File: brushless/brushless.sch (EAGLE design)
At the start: 74 parts, among them Q1 BUK7Y12-40E, Q2 BUK7Y12-40E, Q3 BUK7Y12-40E, Q4 BUK7Y12-40E, Q5 BUK7Y12-40E, Q6 BUK7Y12-40E, X2 MOTOR

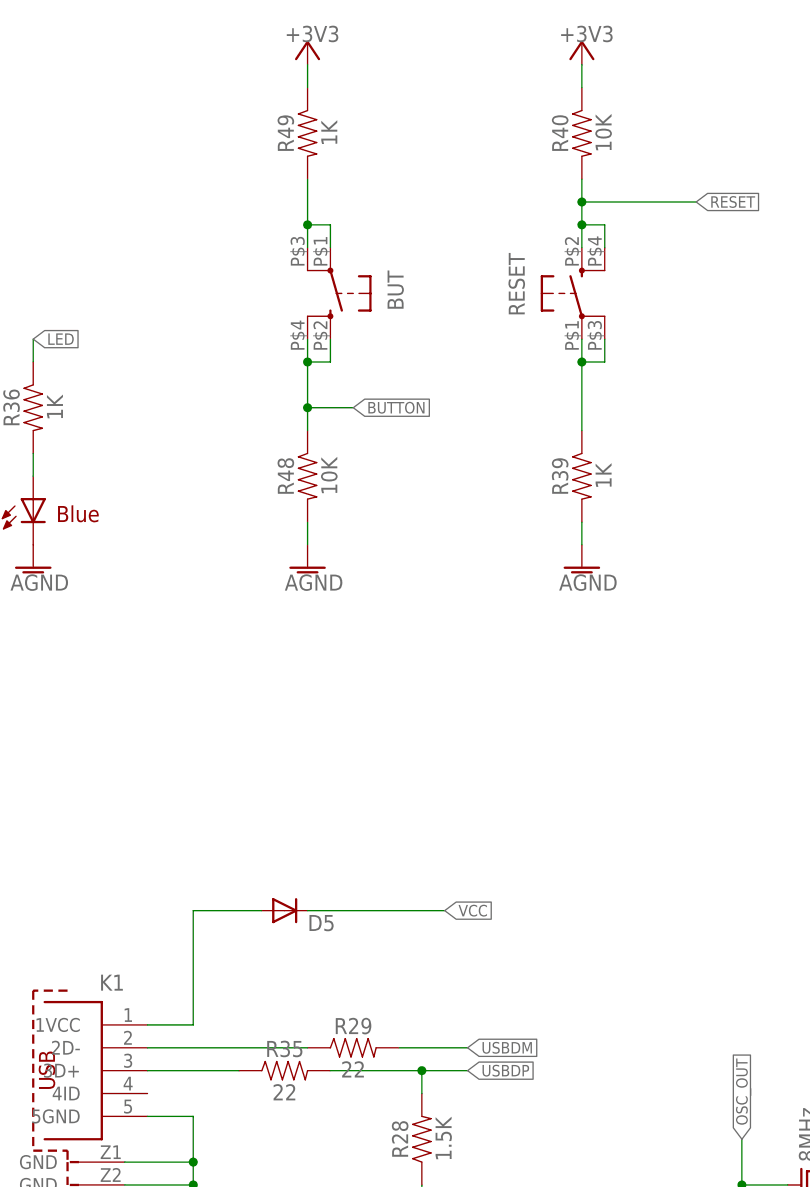
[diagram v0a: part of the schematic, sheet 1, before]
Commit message: brushless board rerouted
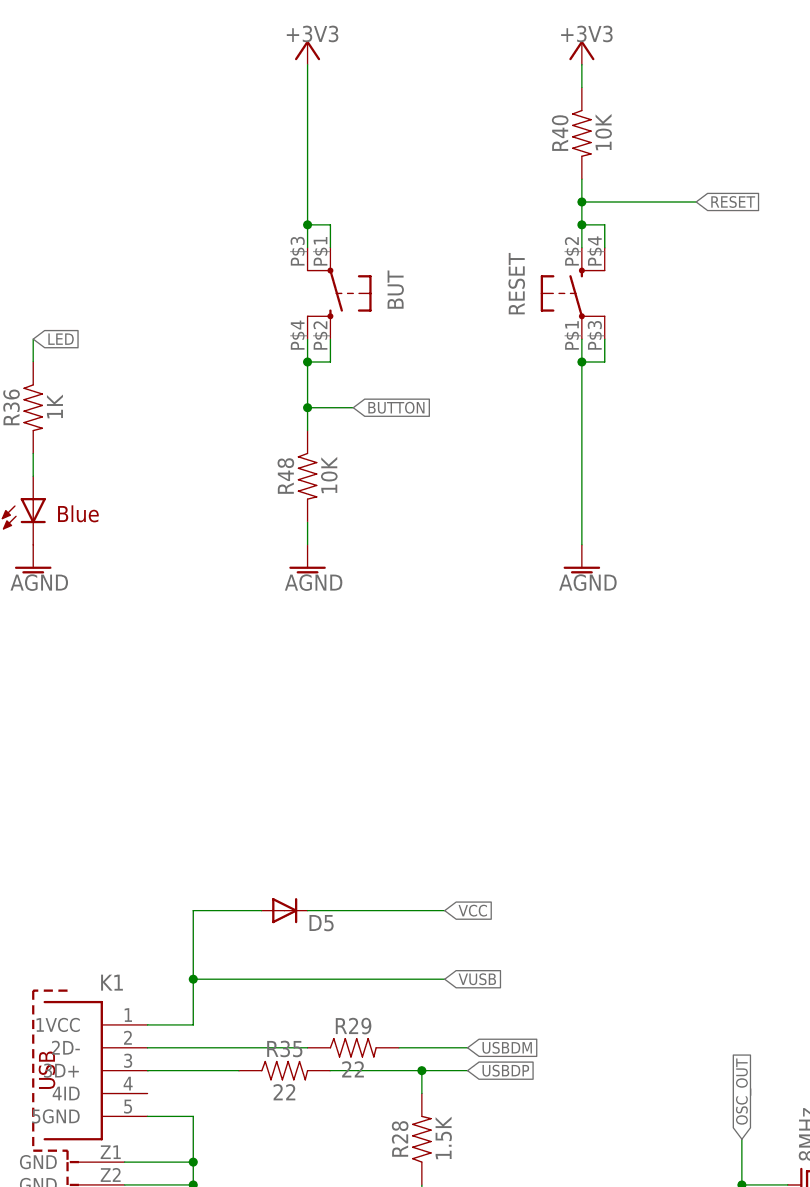
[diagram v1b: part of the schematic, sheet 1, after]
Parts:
- removed R39, R49: 1K, SparkFun-Resistors:RESISTOR0805
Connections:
- removed net N$1: R39.1, RESET.1, RESET.3
- removed net N$26: BUT.1, BUT.3, R49.2
- removed net VUSB1: D12.A
- net +3V3: now also BUT.1, BUT.3; no longer R49.1
- net AGND: now also RESET.1, RESET.3; no longer R39.2
- net VUSB: now also D12.A
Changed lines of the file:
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@@
-<attribute name="FARNELL" value="2446904"/>
-</part>
-<part name="R39" library="SparkFun-Resistors" deviceset="RESISTOR" device="0805" value="1K">
 <attribute name="FARNELL" value="2446904"/>
 </part>
@@
 <part name="R48" library="SparkFun-Resistors" deviceset="RESISTOR" device="0805" value="10K">
 <attribute name="FARNELL" value="2447553"/>
-</part>
-<part name="R49" library="SparkFun-Resistors" deviceset="RESISTOR" device="0805" value="1K">
-<attribute name="FARNELL" value="2446904"/>
 </part>
 <part name="R50" library="SparkFun-Resistors" deviceset="RESISTOR" device="0805" value="10K">
@@
 <attribute name="FARNELL" x="-63.5" y="40.64" size="1.778" layer="96" rot="MR270" display="off"/>
 </instance>
-<instance part="R39" gate="G$1" x="-2.54" y="33.02" rot="MR270">
-<attribute name="FARNELL" x="-2.54" y="33.02" size="1.778" layer="96" rot="MR270" display="off"/>
-</instance>
 <instance part="R40" gate="G$1" x="-2.54" y="71.12" rot="MR270">
 <attribute name="FARNELL" x="-2.54" y="71.12" size="1.778" layer="96" rot="MR270" display="off"/>
@@
 <instance part="R48" gate="G$1" x="-33.02" y="33.02" rot="MR270">
 <attribute name="FARNELL" x="-33.02" y="33.02" size="1.778" layer="96" rot="MR270" display="off"/>
-</instance>
-<instance part="R49" gate="G$1" x="-33.02" y="71.12" rot="MR270">
-<attribute name="FARNELL" x="-33.02" y="71.12" size="1.778" layer="96" rot="MR270" display="off"/>
 </instance>
 <instance part="R50" gate="G$1" x="-20.32" y="-55.88" rot="MR90">
@@
 <segment>
 <wire x1="-50.8" y1="-27.94" x2="-45.72" y2="-27.94" width="0.1524" layer="91"/>
-<wire x1="-45.72" y1="-27.94" x2="-45.72" y2="-15.24" width="0.1524" layer="91"/>
+<wire x1="-45.72" y1="-27.94" x2="-45.72" y2="-22.86" width="0.1524" layer="91"/>
 <pinref part="K1" gate="G$1" pin="1VCC"/>
 <pinref part="D5" gate="G$1" pin="A"/>
+<wire x1="-45.72" y1="-22.86" x2="-45.72" y2="-15.24" width="0.1524" layer="91"/>
 <wire x1="-45.72" y1="-15.24" x2="-38.1" y2="-15.24" width="0.1524" layer="91"/>
+<wire x1="-45.72" y1="-22.86" x2="-17.78" y2="-22.86" width="0.1524" layer="91"/>
+<junction x="-45.72" y="-22.86"/>
+<label x="-17.78" y="-22.86" size="1.27" layer="95" xref="yes"/>
 </segment>
 </net>
@@
 <pinref part="OSC" gate="G$1" pin="1"/>
 <pinref part="C20" gate="G$1" pin="2"/>
-</segment>
-</net>
-<net name="N$26" class="0">
-<segment>
-<wire x1="-30.48" y1="58.42" x2="-30.48" y2="60.96" width="0.1524" layer="91"/>
-<wire x1="-30.48" y1="60.96" x2="-33.02" y2="60.96" width="0.1524" layer="91"/>
-<wire x1="-33.02" y1="60.96" x2="-33.02" y2="58.42" width="0.1524" layer="91"/>
-<wire x1="-33.02" y1="60.96" x2="-33.02" y2="66.04" width="0.1524" layer="91"/>
-<junction x="-33.02" y="60.96"/>
-<pinref part="BUT" gate="G$1" pin="1"/>
-<pinref part="BUT" gate="G$1" pin="3"/>
-<pinref part="R49" gate="G$1" pin="2"/>
 </segment>
 </net>
@@
 <segment>
 <pinref part="3.3/4.5D" gate="G$1" pin="+3V3"/>
-<wire x1="-33.02" y1="78.74" x2="-33.02" y2="76.2" width="0.1524" layer="91"/>
-<pinref part="R49" gate="G$1" pin="1"/>
+<wire x1="-30.48" y1="58.42" x2="-30.48" y2="60.96" width="0.1524" layer="91"/>
+<wire x1="-30.48" y1="60.96" x2="-33.02" y2="60.96" width="0.1524" layer="91"/>
+<wire x1="-33.02" y1="60.96" x2="-33.02" y2="58.42" width="0.1524" layer="91"/>
+<junction x="-33.02" y="60.96"/>
+<pinref part="BUT" gate="G$1" pin="1"/>
+<pinref part="BUT" gate="G$1" pin="3"/>
+<wire x1="-33.02" y1="60.96" x2="-33.02" y2="78.74" width="0.1524" layer="91"/>
 </segment>
 </net>
@@
 </segment>
 <segment>
-<pinref part="R39" gate="G$1" pin="2"/>
 <pinref part="AGND2" gate="VR1" pin="AGND"/>
-<wire x1="-2.54" y1="25.4" x2="-2.54" y2="27.94" width="0.1524" layer="91"/>
+<pinref part="RESET" gate="G$1" pin="3"/>
+<wire x1="0" y1="48.26" x2="0" y2="45.72" width="0.1524" layer="91"/>
+<wire x1="-2.54" y1="48.26" x2="-2.54" y2="45.72" width="0.1524" layer="91"/>
+<pinref part="RESET" gate="G$1" pin="1"/>
+<wire x1="0" y1="45.72" x2="-2.54" y2="45.72" width="0.1524" layer="91"/>
+<junction x="-2.54" y="45.72"/>
+<wire x1="-2.54" y1="45.72" x2="-2.54" y2="25.4" width="0.1524" layer="91"/>
 </segment>
 <segment>
@@
 <pinref part="C12" gate="G$1" pin="1"/>
 <pinref part="AGND10" gate="VR1" pin="AGND"/>
-</segment>
-</net>
-<net name="N$1" class="0">
-<segment>
-<pinref part="RESET" gate="G$1" pin="3"/>
-<wire x1="0" y1="48.26" x2="0" y2="45.72" width="0.1524" layer="91"/>
-<wire x1="-2.54" y1="48.26" x2="-2.54" y2="45.72" width="0.1524" layer="91"/>
-<wire x1="-2.54" y1="45.72" x2="-2.54" y2="38.1" width="0.1524" layer="91"/>
-<pinref part="RESET" gate="G$1" pin="1"/>
-<pinref part="R39" gate="G$1" pin="1"/>
-<wire x1="0" y1="45.72" x2="-2.54" y2="45.72" width="0.1524" layer="91"/>
-<junction x="-2.54" y="45.72"/>
 </segment>
 </net>
@@
 </segment>
 </net>
-<net name="VUSB1" class="0">
+<net name="VUSB" class="0">
 <segment>
 <pinref part="D12" gate="G$1" pin="A"/>

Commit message: Values
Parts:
- C1, C2, C3: value 10µF -> 1µF
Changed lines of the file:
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@@
 <attribute name="FARNELL" value="8638730"/>
 </part>
-<part name="C1" library="SparkFun-Capacitors" deviceset="0.33UF/330NF" device="-0805-50V-10%" value="10µF">
+<part name="C1" library="SparkFun-Capacitors" deviceset="0.33UF/330NF" device="-0805-50V-10%" value="1µF">
 <attribute name="FARNELL" value="2528772"/>
 </part>
@@
 <attribute name="FARNELL" value="8638730"/>
 </part>
-<part name="C2" library="SparkFun-Capacitors" deviceset="0.33UF/330NF" device="-0805-50V-10%" value="10µF">
+<part name="C2" library="SparkFun-Capacitors" deviceset="0.33UF/330NF" device="-0805-50V-10%" value="1µF">
 <attribute name="FARNELL" value="2528772"/>
 </part>
@@
 <attribute name="FARNELL" value="8638730"/>
 </part>
-<part name="C3" library="SparkFun-Capacitors" deviceset="0.33UF/330NF" device="-0805-50V-10%" value="10µF">
+<part name="C3" library="SparkFun-Capacitors" deviceset="0.33UF/330NF" device="-0805-50V-10%" value="1µF">
 <attribute name="FARNELL" value="2528772"/>
 </part>

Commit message: Passive values
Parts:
- C11: value 1000pF -> 1uF
- C13: value 1000pF -> 100nF
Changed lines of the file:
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@@
 <attribute name="FARNELL" value="2496935"/>
 </part>
-<part name="C11" library="SparkFun-Passives" deviceset="CAP" device="0805" value="1000pF">
+<part name="C11" library="SparkFun-Passives" deviceset="CAP" device="0805" value="1uF">
 <attribute name="FARNELL" value="2496935"/>
 </part>
-<part name="C13" library="SparkFun-Passives" deviceset="CAP" device="0805" value="1000pF">
+<part name="C13" library="SparkFun-Passives" deviceset="CAP" device="0805" value="100nF">
 <attribute name="FARNELL" value="2496935"/>
 </part>

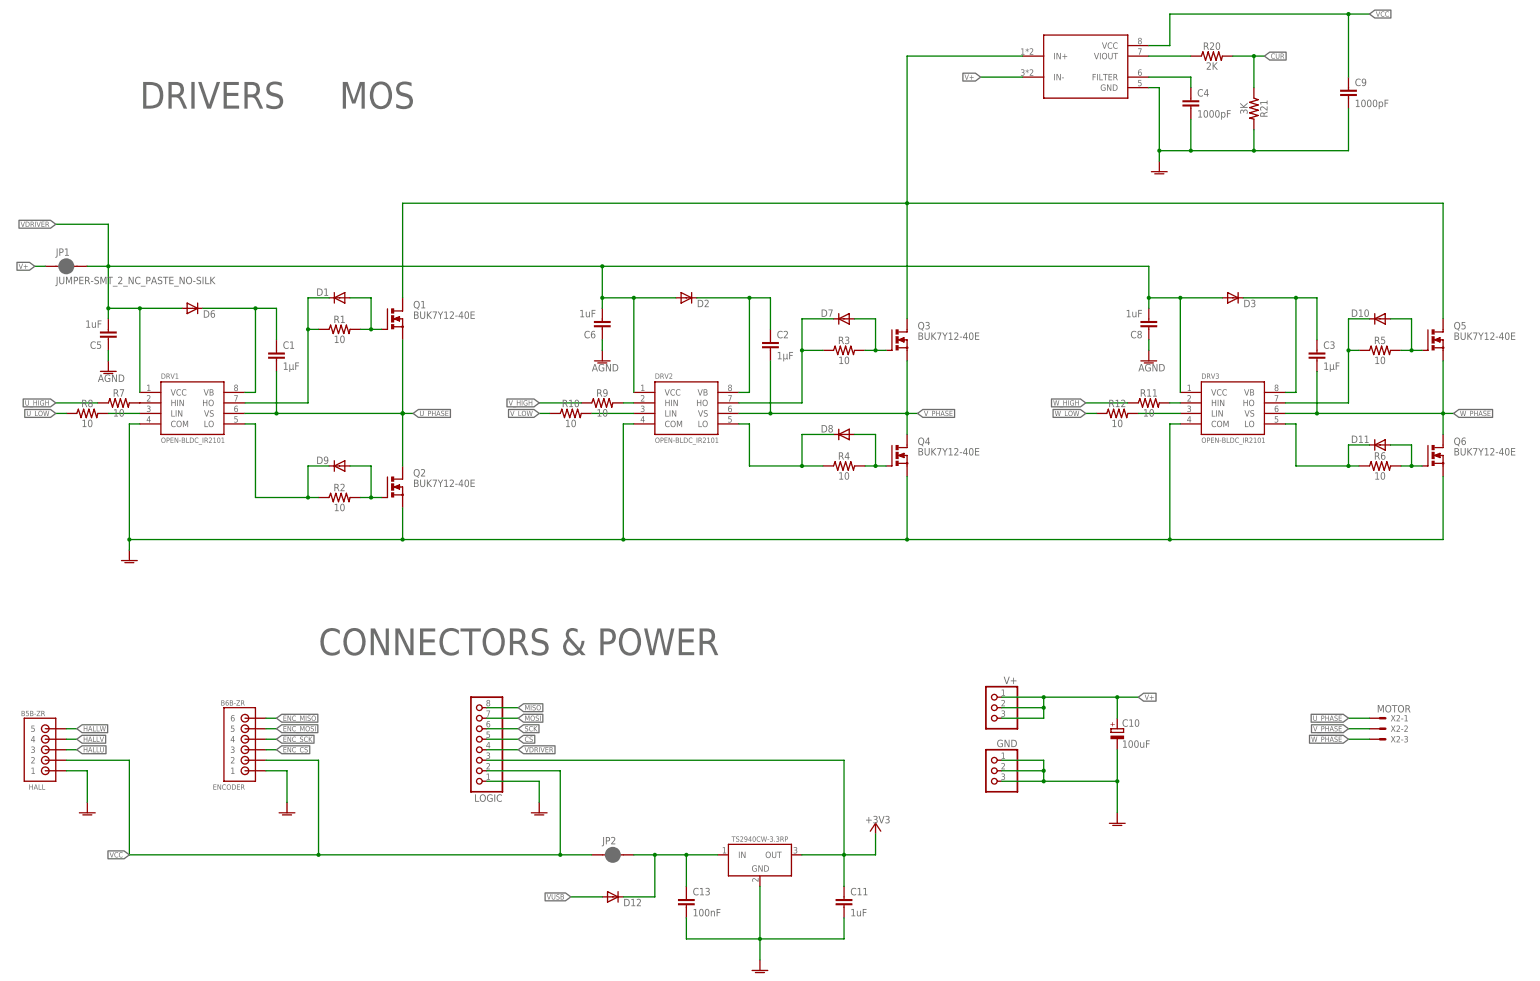
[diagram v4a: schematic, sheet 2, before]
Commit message: Improving values indications
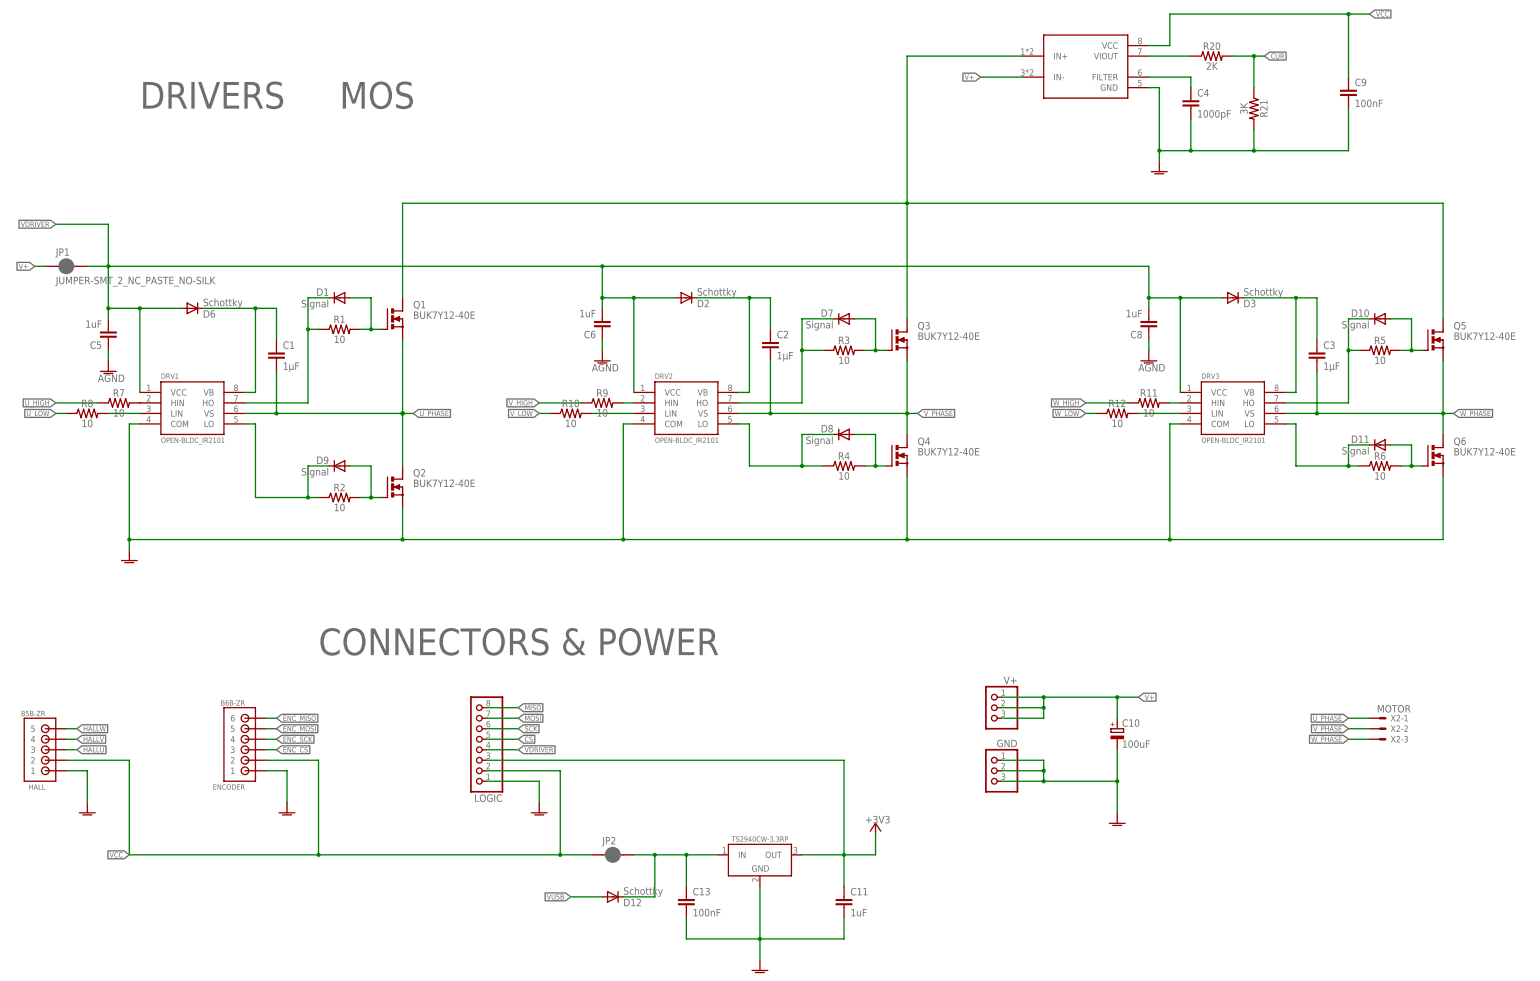
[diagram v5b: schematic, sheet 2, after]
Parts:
- C9: value 1000pF -> 100nF
- D1, D10, D11, D7, D8, D9: value (none) -> Signal; FARNELL 8737843RL -> 1843678RL
- D12, D2, D3, D5, D6: value (none) -> Schottky; FARNELL 8737843RL -> 2760406
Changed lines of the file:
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@@
 <attribute name="FARNELL" value="1870964"/>
 </part>
-<part name="D5" library="SparkFun-DiscreteSemi" deviceset="DIODE" device="SOD">
-<attribute name="FARNELL" value="8737843RL"/>
+<part name="D5" library="SparkFun-DiscreteSemi" deviceset="DIODE" device="SOD" value="Schottky">
+<attribute name="FARNELL" value="2760406"/>
 </part>
 <part name="JP1" library="SparkFun-Jumpers" deviceset="JUMPER-SMT_2_NC_PASTE" device="_NO-SILK">
@@
 <part name="AGND19" library="supply1" deviceset="AGND" device=""/>
 <part name="AGND20" library="supply1" deviceset="AGND" device=""/>
-<part name="C9" library="SparkFun-Passives" deviceset="CAP" device="0805" value="1000pF">
+<part name="C9" library="SparkFun-Passives" deviceset="CAP" device="0805" value="100nF">
 <attribute name="FARNELL" value="2496935"/>
 </part>
@@
 </part>
 <part name="3.3/4.5D3" library="supply1" deviceset="+3V3" device=""/>
-<part name="D6" library="SparkFun-DiscreteSemi" deviceset="DIODE" device="SOD">
-<attribute name="FARNELL" value="8737843RL"/>
+<part name="D6" library="SparkFun-DiscreteSemi" deviceset="DIODE" device="SOD" value="Schottky">
+<attribute name="FARNELL" value="2760406"/>
 </part>
-<part name="D1" library="SparkFun-DiscreteSemi" deviceset="DIODE" device="SOD">
-<attribute name="FARNELL" value="8737843RL"/>
+<part name="D1" library="SparkFun-DiscreteSemi" deviceset="DIODE" device="SOD" value="Signal">
+<attribute name="FARNELL" value="1843678RL"/>
 </part>
-<part name="D2" library="SparkFun-DiscreteSemi" deviceset="DIODE" device="SOD">
-<attribute name="FARNELL" value="8737843RL"/>
+<part name="D2" library="SparkFun-DiscreteSemi" deviceset="DIODE" device="SOD" value="Schottky">
+<attribute name="FARNELL" value="2760406"/>
 </part>
-<part name="D7" library="SparkFun-DiscreteSemi" deviceset="DIODE" device="SOD">
-<attribute name="FARNELL" value="8737843RL"/>
+<part name="D7" library="SparkFun-DiscreteSemi" deviceset="DIODE" device="SOD" value="Signal">
+<attribute name="FARNELL" value="1843678RL"/>
 </part>
-<part name="D8" library="SparkFun-DiscreteSemi" deviceset="DIODE" device="SOD">
-<attribute name="FARNELL" value="8737843RL"/>
+<part name="D8" library="SparkFun-DiscreteSemi" deviceset="DIODE" device="SOD" value="Signal">
+<attribute name="FARNELL" value="1843678RL"/>
 </part>
-<part name="D9" library="SparkFun-DiscreteSemi" deviceset="DIODE" device="SOD">
-<attribute name="FARNELL" value="8737843RL"/>
+<part name="D9" library="SparkFun-DiscreteSemi" deviceset="DIODE" device="SOD" value="Signal">
+<attribute name="FARNELL" value="1843678RL"/>
 </part>
-<part name="D3" library="SparkFun-DiscreteSemi" deviceset="DIODE" device="SOD">
-<attribute name="FARNELL" value="8737843RL"/>
+<part name="D3" library="SparkFun-DiscreteSemi" deviceset="DIODE" device="SOD" value="Schottky">
+<attribute name="FARNELL" value="2760406"/>
 </part>
-<part name="D10" library="SparkFun-DiscreteSemi" deviceset="DIODE" device="SOD">
-<attribute name="FARNELL" value="8737843RL"/>
+<part name="D10" library="SparkFun-DiscreteSemi" deviceset="DIODE" device="SOD" value="Signal">
+<attribute name="FARNELL" value="1843678RL"/>
 </part>
-<part name="D11" library="SparkFun-DiscreteSemi" deviceset="DIODE" device="SOD">
-<attribute name="FARNELL" value="8737843RL"/>
+<part name="D11" library="SparkFun-DiscreteSemi" deviceset="DIODE" device="SOD" value="Signal">
+<attribute name="FARNELL" value="1843678RL"/>
 </part>
-<part name="D12" library="SparkFun-DiscreteSemi" deviceset="DIODE" device="SOD">
-<attribute name="FARNELL" value="8737843RL"/>
+<part name="D12" library="SparkFun-DiscreteSemi" deviceset="DIODE" device="SOD" value="Schottky">
+<attribute name="FARNELL" value="2760406"/>
 </part>
 <part name="R7" library="SparkFun-Resistors" deviceset="RESISTOR" device="0805" value="10">
